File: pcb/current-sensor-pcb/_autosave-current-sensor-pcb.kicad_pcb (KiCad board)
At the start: 2 copper layers, 35 x 45.2 mm, 17 parts, among them U1 TLI4971A050T5UE0001XUMA1

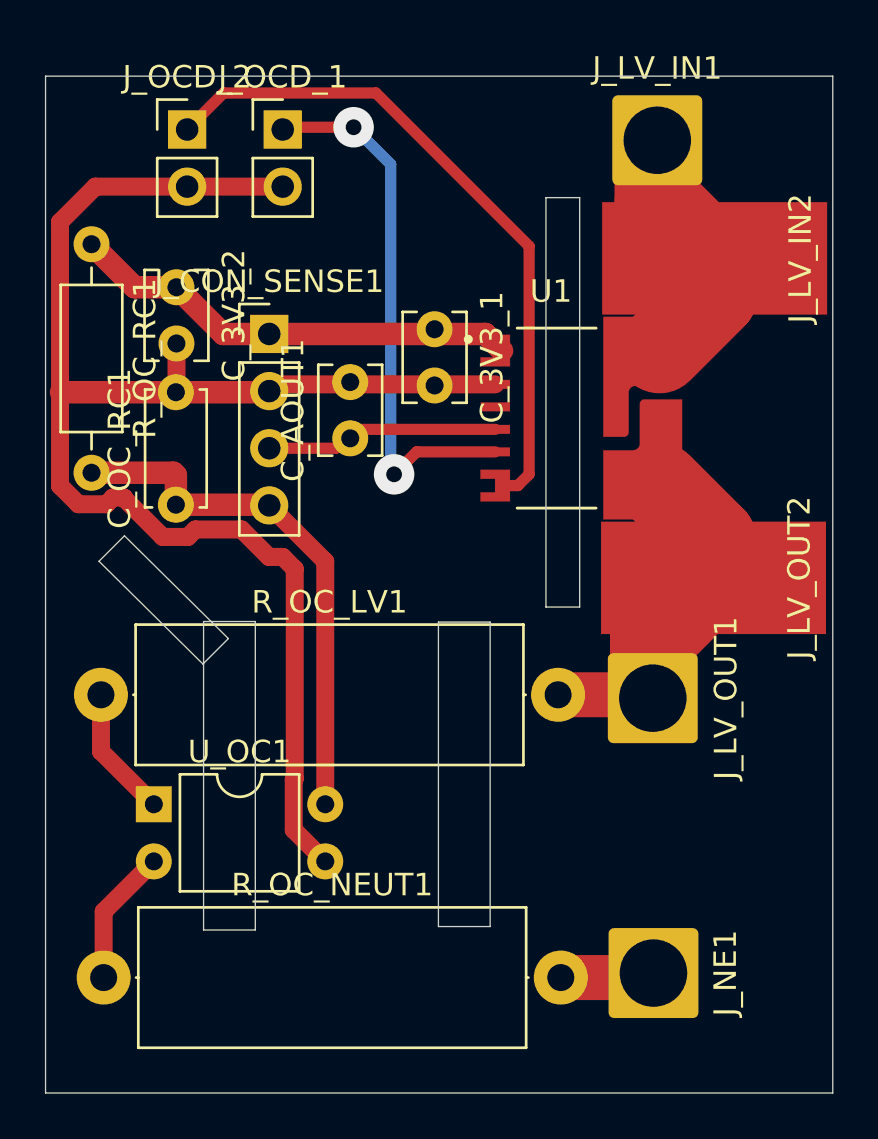
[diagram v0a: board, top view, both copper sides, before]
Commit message: Slight refactor of contator components to support more compact layout
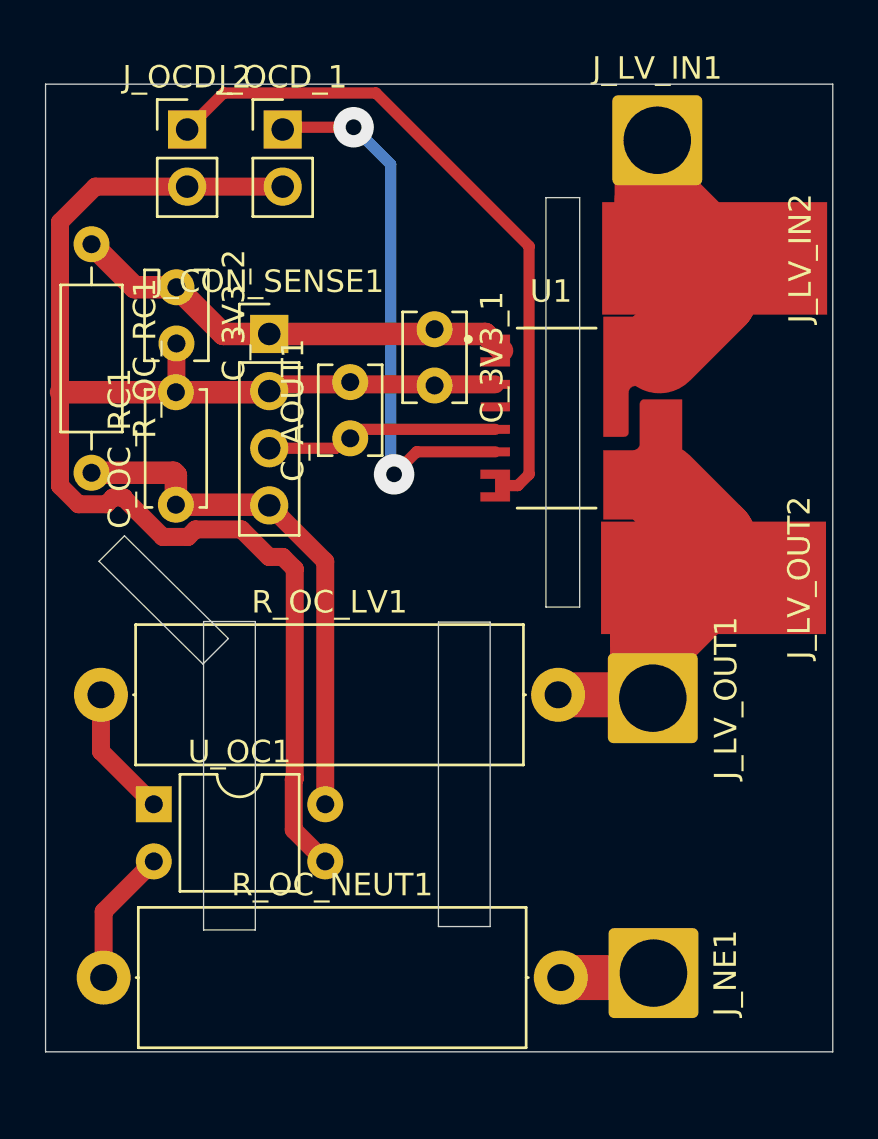
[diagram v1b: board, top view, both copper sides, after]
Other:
- board size 35 x 45.2 mm -> 35 x 43 mm
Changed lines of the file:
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@@
 	)
 	(gr_rect
-		(start 0.1114 -0.1534)
-		(end 35.1044 45.0466)
+		(start 0.1114 0.2022)
+		(end 35.1044 43.2178)
 		(stroke
 			(width 0.05)
